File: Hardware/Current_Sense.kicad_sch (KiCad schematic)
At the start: 39 parts, among them IC2 INA241A4IDR, IC3 AMC1350DWVR, J6 Scrut Conn, SW4 Scrut Select, U10 TLV9002QDRQ1, U9 REF35125QDBVR

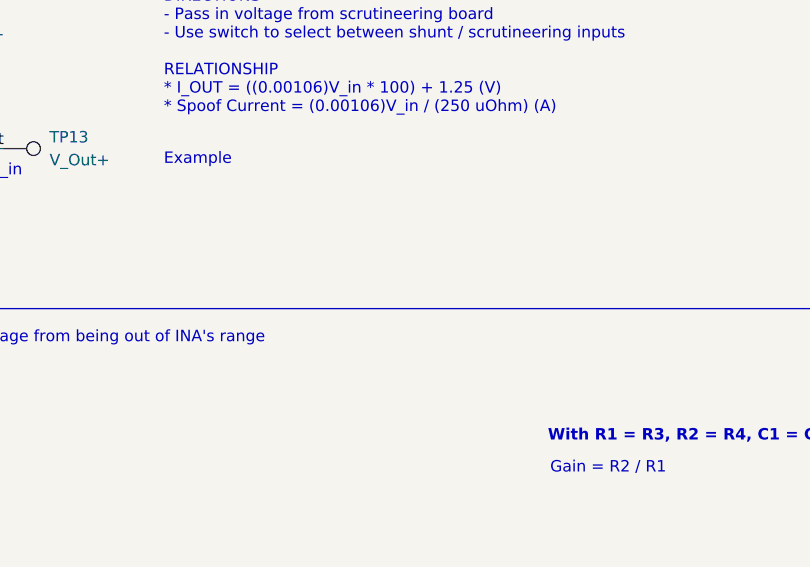
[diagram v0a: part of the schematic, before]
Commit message: post review council sch changes: shielded connectors, removed SHDN resistor, diode OR for boot, standardized resistors
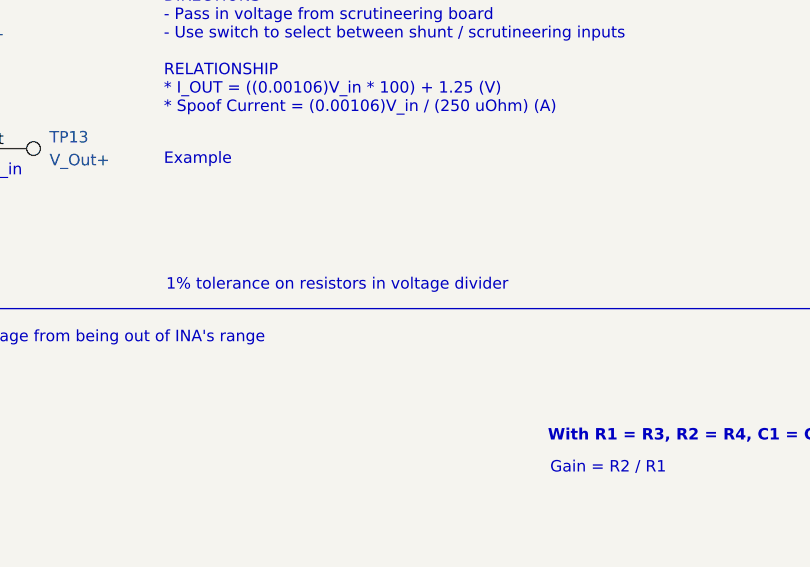
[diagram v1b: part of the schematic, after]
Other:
- note added: "1% tolerance on resistors in voltage divider"
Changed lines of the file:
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@@
+		)
+	)
+	(text "1% tolerance on resistors in voltage divider"
+		(exclude_from_sim no)
+		(at 203.454 60.198 0)
+		(effects
+			(font
+				(size 1.27 1.27)
+				(color 255 8 29 1)
+			)
+			(justify left top)
 		)
 	)

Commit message: starting routing i think
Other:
- note added: "Vref = 1.25 V | Shunt = 250 uOhm | Gain = ~100 V/V (100 * 0.4 * 2.49) Shunt * gain = 250 uOhm * 100 V/V = 0.025"
- note removed: "Vref = 1.25 V | Shunt = 250 uOhm | Gain = 100 V/V Shunt * gain = 250 uOhm * 100 V/V = 0.025"
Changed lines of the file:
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@@
 	(rectangle
 		(start 93.98 165.1)
-		(end 160.02 195.834)
+		(end 175.26 195.834)
 		(stroke
 			(width 0)
@@
 		)
 	)
-	(text "Vref = 1.25 V | Shunt = 250 uOhm | Gain = 100 V/V\nShunt * gain = 250 uOhm * 100 V/V = 0.025"
+	(text "Vref = 1.25 V | Shunt = 250 uOhm | Gain = ~100 V/V (100 * 0.4 * 2.49)\nShunt * gain = 250 uOhm * 100 V/V = 0.025"
 		(exclude_from_sim no)
 		(at 96.52 190.5 0)

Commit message: added lcsc part numbers
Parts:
- TP10, TP11, TP12, TP13, TP14, TP17, TP18, TP20: now left out of the parts list
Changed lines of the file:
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@@
 		(unit 1)
 		(exclude_from_sim no)
-		(in_bom yes)
+		(in_bom no)
 		(on_board yes)
 		(dnp no)
@@
 		(unit 1)
 		(exclude_from_sim no)
-		(in_bom yes)
+		(in_bom no)
 		(on_board yes)
 		(dnp no)
@@
 		(unit 1)
 		(exclude_from_sim no)
-		(in_bom yes)
+		(in_bom no)
 		(on_board yes)
 		(dnp no)
@@
 		(unit 1)
 		(exclude_from_sim no)
-		(in_bom yes)
+		(in_bom no)
 		(on_board yes)
 		(dnp no)
@@
 		(unit 1)
 		(exclude_from_sim no)
-		(in_bom yes)
+		(in_bom no)
 		(on_board yes)
 		(dnp no)
@@
 		(unit 1)
 		(exclude_from_sim no)
-		(in_bom yes)
+		(in_bom no)
 		(on_board yes)
 		(dnp no)
@@
 		(unit 1)
 		(exclude_from_sim no)
-		(in_bom yes)
+		(in_bom no)
 		(on_board yes)
 		(dnp no)
@@
 		(unit 1)
 		(exclude_from_sim no)
-		(in_bom yes)
+		(in_bom no)
 		(on_board yes)
 		(dnp no)
